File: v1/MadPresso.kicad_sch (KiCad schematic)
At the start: 37 parts, among them J1 Conn_01x07, J2 Conn_01x03, Q1 2N7002, Q2 2N7002, Q3 BC847, U1 LTV-356T, U7 WeMos_mini

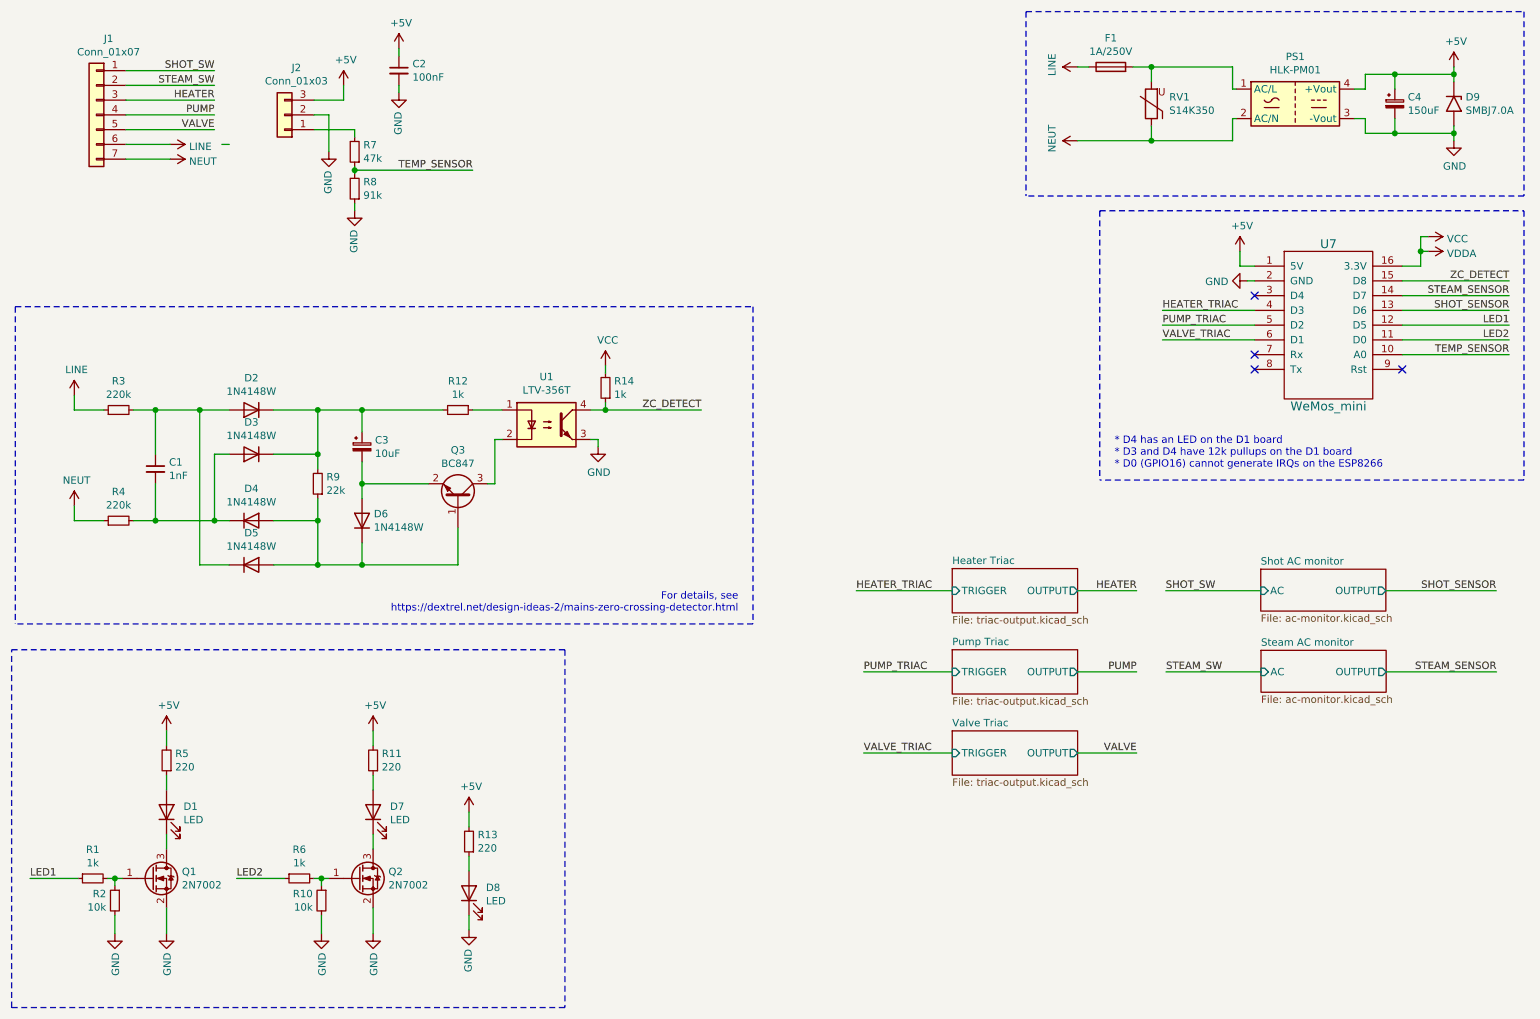
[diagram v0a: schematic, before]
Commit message: Add another blocker C
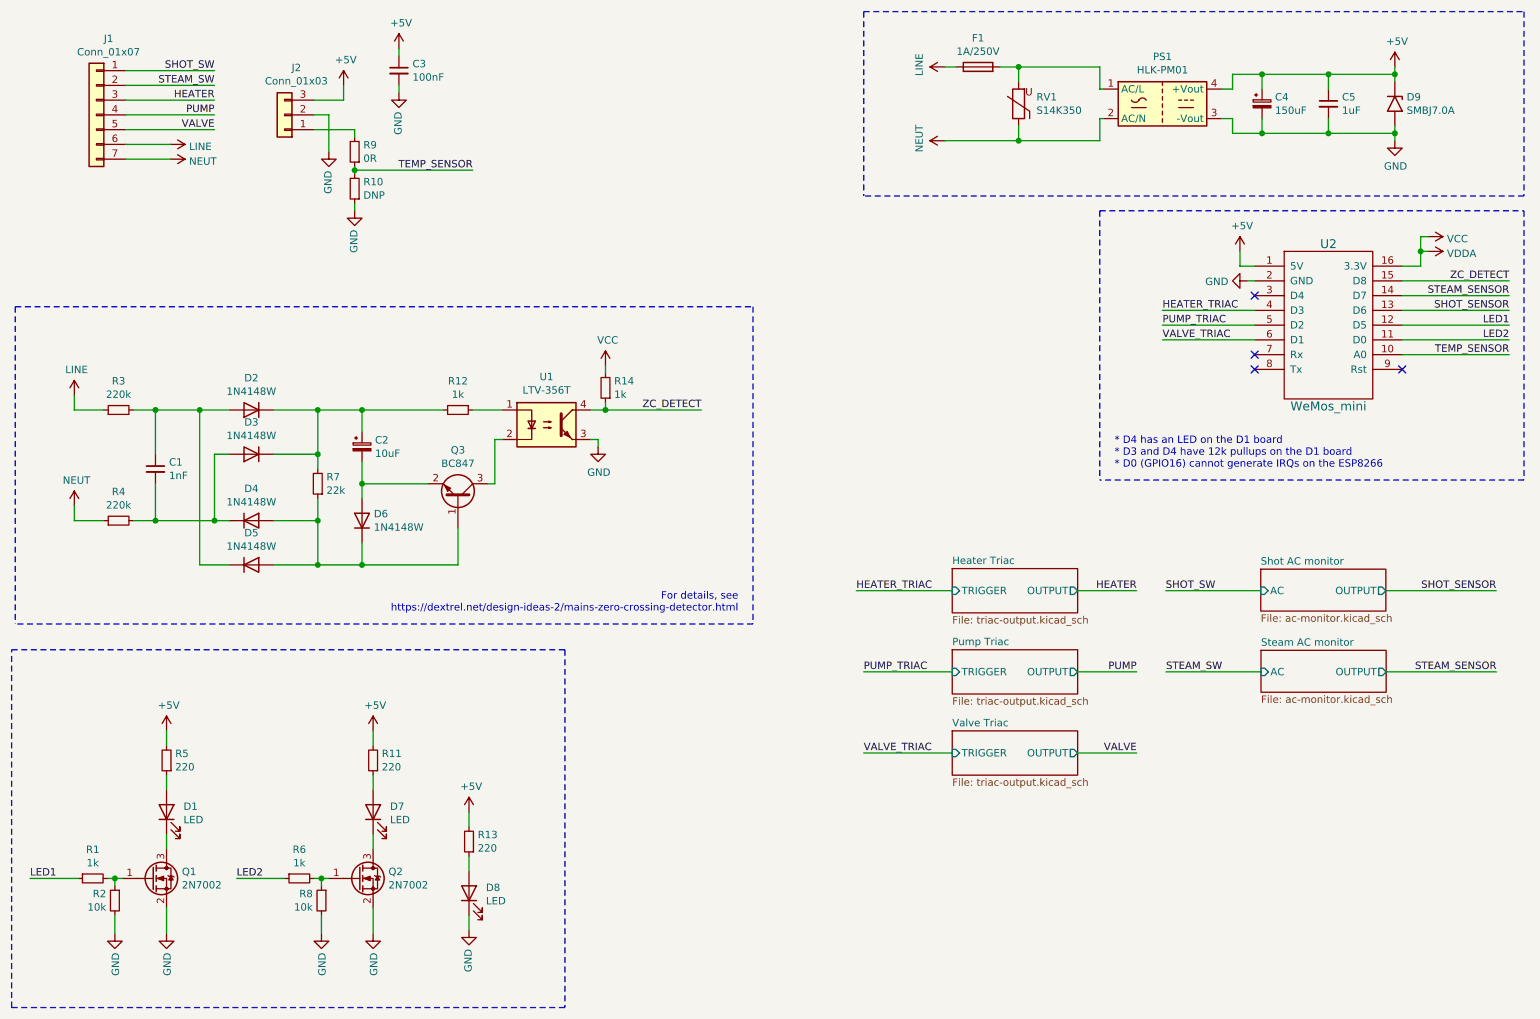
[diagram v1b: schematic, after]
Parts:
- added C5: 1uF, Capacitor_SMD:C_0603_1608Metric_Pad1.05x0.95mm_HandSolder, symbol Device:C_Small
- R10: renamed from R8; value 91k -> DNP
- R9: renamed from R7; value 47k -> 0R
- renumbered C3 to C2, C2 to C3, R9 to R7, R10 to R8, U7 to U2
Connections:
- net +5V: now also C5.1
- net GND: now also C5.2
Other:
- moved on the sheet: C4, D9, F1, PS1, RV1

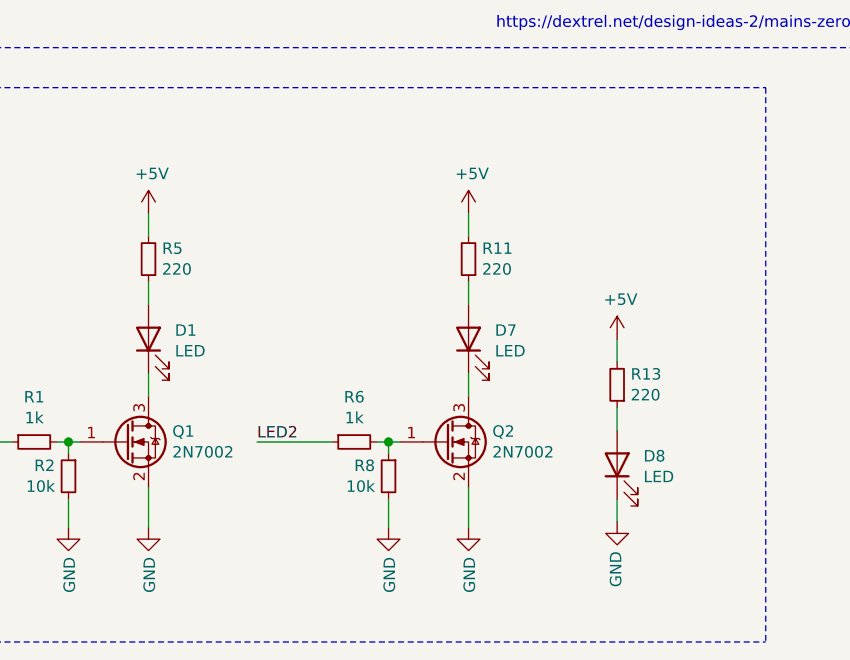
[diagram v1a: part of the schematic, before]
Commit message: some resistor footpring changes
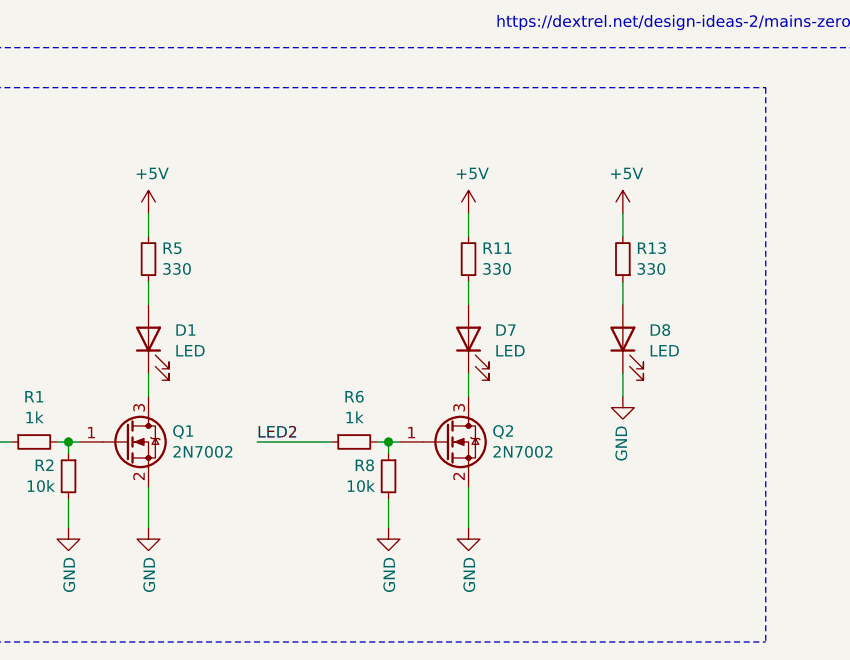
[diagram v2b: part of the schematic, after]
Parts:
- R11, R13, R5: value 220 -> 330
- R3, R4: footprint Resistor_SMD:R_0603_1608Metric_Pad1.05x0.95mm_HandSolder -> Resistor_SMD:R_1206_3216Metric_Pad1.42x1.75mm_HandSolder
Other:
- moved on the sheet: D8, R13
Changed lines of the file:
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@@
   (junction (at 255.905 41.91) (diameter 1.016) (color 0 0 0 0))
   (junction (at 260.35 62.23) (diameter 1.016) (color 0 0 0 0))
-  (no_connect (at 231.775 82.55))
+  (no_connect (at 257.175 82.55))
   (no_connect (at 231.775 80.01))
   (no_connect (at 231.775 69.85))
-  (no_connect (at 257.175 82.55))
+  (no_connect (at 231.775 82.55))
   (wire (pts (xy 20.955 170.18) (xy 29.21 170.18))
     (stroke (width 0) (type solid) (color 0 0 0 0))
@@
     (stroke (width 0) (type solid) (color 0 0 0 0))
   )
-  (wire (pts (xy 96.52 158.75) (xy 96.52 161.29))
-    (stroke (width 0) (type solid) (color 0 0 0 0))
-  )
-  (wire (pts (xy 96.52 166.37) (xy 96.52 168.91))
-    (stroke (width 0) (type solid) (color 0 0 0 0))
-  )
-  (wire (pts (xy 96.52 176.53) (xy 96.52 179.07))
-    (stroke (width 0) (type solid) (color 0 0 0 0))
-  )
   (wire (pts (xy 97.155 89.535) (xy 102.235 89.535))
+    (stroke (width 0) (type solid) (color 0 0 0 0))
+  )
+  (wire (pts (xy 97.155 144.78) (xy 97.155 147.32))
+    (stroke (width 0) (type solid) (color 0 0 0 0))
+  )
+  (wire (pts (xy 97.155 152.4) (xy 97.155 154.94))
+    (stroke (width 0) (type solid) (color 0 0 0 0))
+  )
+  (wire (pts (xy 97.155 162.56) (xy 97.155 165.1))
     (stroke (width 0) (type solid) (color 0 0 0 0))
   )
@@
     )
   )
-  (symbol (lib_id "power:+5V") (at 96.52 158.75 0) (unit 1)
-    (in_bom yes) (on_board yes)
-    (property "Reference" "#PWR016" (id 0) (at 96.52 162.56 0)
-      (effects (font (size 1.27 1.27)) hide)
-    )
-    (property "Value" "+5V" (id 1) (at 96.901 154.3558 0))
-    (property "Footprint" "" (id 2) (at 96.52 158.75 0)
-      (effects (font (size 1.27 1.27)) hide)
-    )
-    (property "Datasheet" "" (id 3) (at 96.52 158.75 0)
+  (symbol (lib_id "power:+5V") (at 97.155 144.78 0) (unit 1)
+    (in_bom yes) (on_board yes)
+    (property "Reference" "#PWR016" (id 0) (at 97.155 148.59 0)
+      (effects (font (size 1.27 1.27)) hide)
+    )
+    (property "Value" "+5V" (id 1) (at 97.536 140.3858 0))
+    (property "Footprint" "" (id 2) (at 97.155 144.78 0)
+      (effects (font (size 1.27 1.27)) hide)
+    )
+    (property "Datasheet" "" (id 3) (at 97.155 144.78 0)
       (effects (font (size 1.27 1.27)) hide)
     )
@@
     )
   )
-  (symbol (lib_id "power:GND") (at 96.52 179.07 0) (mirror y) (unit 1)
-    (in_bom yes) (on_board yes)
-    (property "Reference" "#PWR017" (id 0) (at 96.52 185.42 0)
-      (effects (font (size 1.27 1.27)) hide)
-    )
-    (property "Value" "GND" (id 1) (at 96.393 182.3212 90)
-      (effects (font (size 1.27 1.27)) (justify right))
-    )
-    (property "Footprint" "" (id 2) (at 96.52 179.07 0)
-      (effects (font (size 1.27 1.27)) hide)
-    )
-    (property "Datasheet" "" (id 3) (at 96.52 179.07 0)
+  (symbol (lib_id "power:GND") (at 97.155 165.1 0) (mirror y) (unit 1)
+    (in_bom yes) (on_board yes)
+    (property "Reference" "#PWR017" (id 0) (at 97.155 171.45 0)
+      (effects (font (size 1.27 1.27)) hide)
+    )
+    (property "Value" "GND" (id 1) (at 97.028 168.3512 90)
+      (effects (font (size 1.27 1.27)) (justify right))
+    )
+    (property "Footprint" "" (id 2) (at 97.155 165.1 0)
+      (effects (font (size 1.27 1.27)) hide)
+    )
+    (property "Datasheet" "" (id 3) (at 97.155 165.1 0)
       (effects (font (size 1.27 1.27)) hide)
     )
@@
     (property "Reference" "R3" (id 0) (at 36.195 84.5566 90))
     (property "Value" "220k" (id 1) (at 36.195 86.868 90))
-    (property "Footprint" "Resistor_SMD:R_0603_1608Metric_Pad1.05x0.95mm_HandSolder" (id 2) (at 36.195 89.535 0)
+    (property "Footprint" "Resistor_SMD:R_1206_3216Metric_Pad1.42x1.75mm_HandSolder" (id 2) (at 36.195 89.535 0)
       (effects (font (size 1.27 1.27)) hide)
     )
@@
     (property "Reference" "R4" (id 0) (at 36.195 103.6066 90))
     (property "Value" "220k" (id 1) (at 36.195 105.918 90))
-    (property "Footprint" "Resistor_SMD:R_0603_1608Metric_Pad1.05x0.95mm_HandSolder" (id 2) (at 36.195 108.585 0)
+    (property "Footprint" "Resistor_SMD:R_1206_3216Metric_Pad1.42x1.75mm_HandSolder" (id 2) (at 36.195 108.585 0)
       (effects (font (size 1.27 1.27)) hide)
     )
@@
       (effects (font (size 1.27 1.27)) (justify right))
     )
-    (property "Value" "220" (id 1) (at 45.9486 151.003 0)
+    (property "Value" "330" (id 1) (at 45.9486 151.003 0)
       (effects (font (size 1.27 1.27)) (justify right))
     )
@@
       (effects (font (size 1.27 1.27)) (justify right))
     )
-    (property "Value" "220" (id 1) (at 81.5086 151.003 0)
+    (property "Value" "330" (id 1) (at 81.5086 151.003 0)
       (effects (font (size 1.27 1.27)) (justify right))
     )
@@
     )
   )
-  (symbol (lib_id "Device:R_Small") (at 96.52 163.83 180) (unit 1)
-    (in_bom yes) (on_board yes)
-    (property "Reference" "R13" (id 0) (at 98.0186 162.6616 0)
-      (effects (font (size 1.27 1.27)) (justify right))
-    )
-    (property "Value" "220" (id 1) (at 98.0186 164.973 0)
-      (effects (font (size 1.27 1.27)) (justify right))
-    )
-    (property "Footprint" "Resistor_SMD:R_0603_1608Metric_Pad1.05x0.95mm_HandSolder" (id 2) (at 96.52 163.83 0)
-      (effects (font (size 1.27 1.27)) hide)
-    )
-    (property "Datasheet" "~" (id 3) (at 96.52 163.83 0)
+  (symbol (lib_id "Device:R_Small") (at 97.155 149.86 180) (unit 1)
+    (in_bom yes) (on_board yes)
+    (property "Reference" "R13" (id 0) (at 98.6536 148.6916 0)
+      (effects (font (size 1.27 1.27)) (justify right))
+    )
+    (property "Value" "330" (id 1) (at 98.6536 151.003 0)
+      (effects (font (size 1.27 1.27)) (justify right))
+    )
+    (property "Footprint" "Resistor_SMD:R_0603_1608Metric_Pad1.05x0.95mm_HandSolder" (id 2) (at 97.155 149.86 0)
+      (effects (font (size 1.27 1.27)) hide)
+    )
+    (property "Datasheet" "~" (id 3) (at 97.155 149.86 0)
       (effects (font (size 1.27 1.27)) hide)
     )
@@
     )
   )
-  (symbol (lib_id "Device:LED") (at 96.52 172.72 90) (unit 1)
-    (in_bom yes) (on_board yes)
-    (property "Reference" "D8" (id 0) (at 99.4411 171.7611 90)
-      (effects (font (size 1.27 1.27)) (justify right))
-    )
-    (property "Value" "LED" (id 1) (at 99.4411 174.0598 90)
-      (effects (font (size 1.27 1.27)) (justify right))
-    )
-    (property "Footprint" "LED_SMD:LED_0805_2012Metric_Pad1.15x1.40mm_HandSolder" (id 2) (at 96.52 172.72 0)
-      (effects (font (size 1.27 1.27)) hide)
-    )
-    (property "Datasheet" "~" (id 3) (at 96.52 172.72 0)
+  (symbol (lib_id "Device:LED") (at 97.155 158.75 90) (unit 1)
+    (in_bom yes) (on_board yes)
+    (property "Reference" "D8" (id 0) (at 100.0761 157.7911 90)
+      (effects (font (size 1.27 1.27)) (justify right))
+    )
+    (property "Value" "LED" (id 1) (at 100.0761 160.0898 90)
+      (effects (font (size 1.27 1.27)) (justify right))
+    )
+    (property "Footprint" "LED_SMD:LED_0805_2012Metric_Pad1.15x1.40mm_HandSolder" (id 2) (at 97.155 158.75 0)
+      (effects (font (size 1.27 1.27)) hide)
+    )
+    (property "Datasheet" "~" (id 3) (at 97.155 158.75 0)
       (effects (font (size 1.27 1.27)) hide)
     )
@@
     )
     (path "/00000000-0000-0000-0000-00005ffbc358"
-      (reference "R3") (unit 1) (value "220k") (footprint "Resistor_SMD:R_0603_1608Metric_Pad1.05x0.95mm_HandSolder")
+      (reference "R3") (unit 1) (value "220k") (footprint "Resistor_SMD:R_1206_3216Metric_Pad1.42x1.75mm_HandSolder")
     )
     (path "/00000000-0000-0000-0000-00005ffbc6cb"
-      (reference "R4") (unit 1) (value "220k") (footprint "Resistor_SMD:R_0603_1608Metric_Pad1.05x0.95mm_HandSolder")
+      (reference "R4") (unit 1) (value "220k") (footprint "Resistor_SMD:R_1206_3216Metric_Pad1.42x1.75mm_HandSolder")
     )
     (path "/40bee37e-5bc8-49d6-a87e-ada61f3c8e70"
-      (reference "R5") (unit 1) (value "220") (footprint "Resistor_SMD:R_0603_1608Metric_Pad1.05x0.95mm_HandSolder")
+      (reference "R5") (unit 1) (value "330") (footprint "Resistor_SMD:R_0603_1608Metric_Pad1.05x0.95mm_HandSolder")
     )
     (path "/9cc82a32-fc0d-4a0b-90ec-76ffa53d254f"
@@
     )
     (path "/3fb4a516-57d9-4ea7-9cb0-5dfafb5be43e"
-      (reference "R11") (unit 1) (value "220") (footprint "Resistor_SMD:R_0603_1608Metric_Pad1.05x0.95mm_HandSolder")
+      (reference "R11") (unit 1) (value "330") (footprint "Resistor_SMD:R_0603_1608Metric_Pad1.05x0.95mm_HandSolder")
     )
     (path "/00000000-0000-0000-0000-00005ffbac90"
@@
     )
     (path "/693ef66e-7ef6-4b62-a2b7-57a53077b15e"
-      (reference "R13") (unit 1) (value "220") (footprint "Resistor_SMD:R_0603_1608Metric_Pad1.05x0.95mm_HandSolder")
+      (reference "R13") (unit 1) (value "330") (footprint "Resistor_SMD:R_0603_1608Metric_Pad1.05x0.95mm_HandSolder")
     )
     (path "/00000000-0000-0000-0000-00005ffe1cf2"

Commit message: more work
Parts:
- F1: value 1A/250V -> 0.1A/250V
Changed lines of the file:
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@@
     (in_bom yes) (on_board yes)
     (property "Reference" "F1" (id 0) (at 184.15 25.5078 90))
-    (property "Value" "1A/250V" (id 1) (at 184.15 27.813 90))
+    (property "Value" "0.1A/250V" (id 1) (at 184.15 27.813 90))
     (property "Footprint" "Fuse:Fuseholder_Cylinder-5x20mm_Schurter_0031_8201_Horizontal_Open" (id 2) (at 184.15 32.258 90)
       (effects (font (size 1.27 1.27)) hide)
@@
     )
     (path "/7c0f56a1-0f85-4240-bbd4-7f7fbc559178"
-      (reference "F1") (unit 1) (value "1A/250V") (footprint "Fuse:Fuseholder_Cylinder-5x20mm_Schurter_0031_8201_Horizontal_Open")
+      (reference "F1") (unit 1) (value "0.1A/250V") (footprint "Fuse:Fuseholder_Cylinder-5x20mm_Schurter_0031_8201_Horizontal_Open")
     )
     (path "/00000000-0000-0000-0000-00005f95d6b9"
